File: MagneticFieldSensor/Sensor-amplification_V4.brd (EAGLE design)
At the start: 100 x 48.9 mm, 52 parts

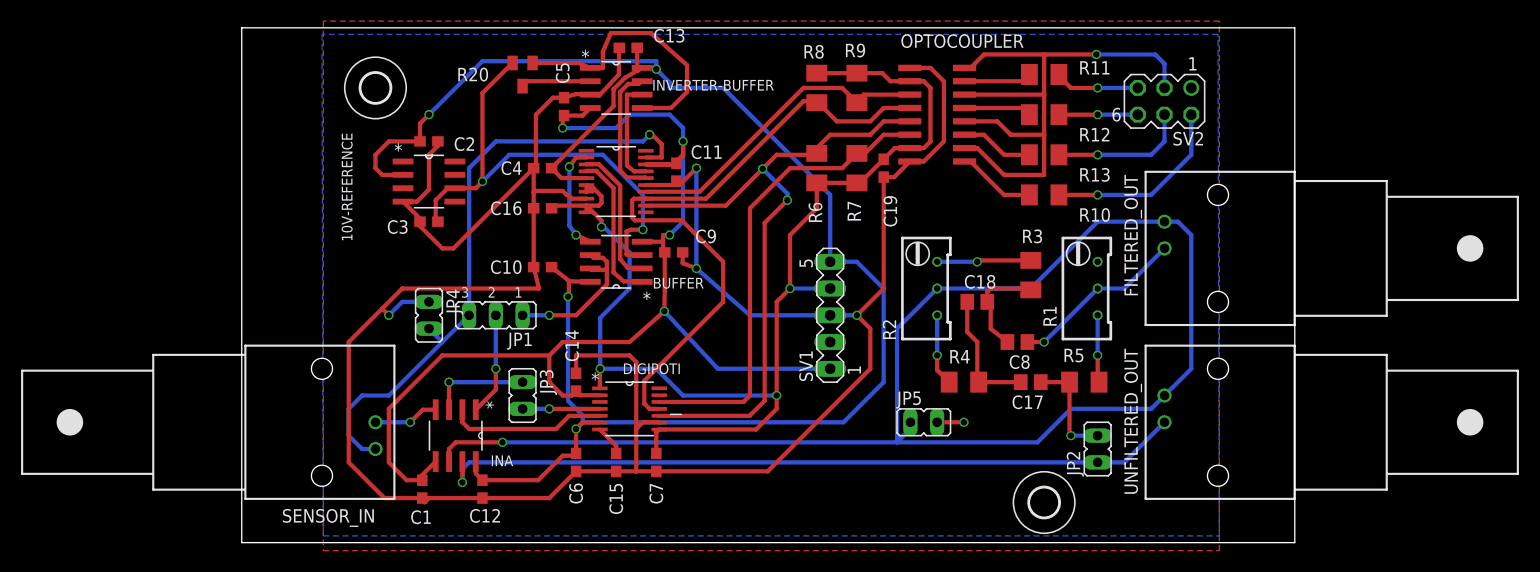
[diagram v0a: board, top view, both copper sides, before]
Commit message: made the board compatible with the PCB rules.
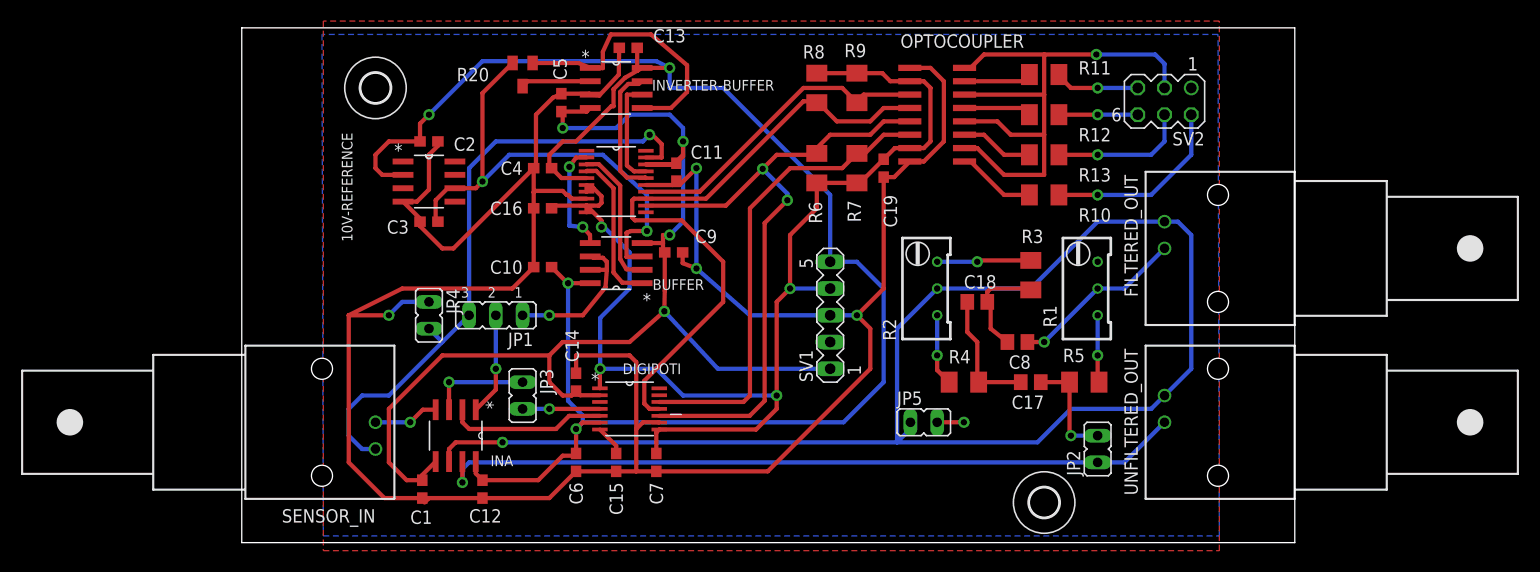
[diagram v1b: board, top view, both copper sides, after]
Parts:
- moved C5 0.46 mm to (30.4, 39.2)
- moved BUFFER 0.13 mm to (35.6, 24.0)
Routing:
- net +15V: track 166.1 -> 168.5 mm
- net AGND: track 247.7 -> 250.0 mm
- net N$9: track 46.4 -> 47.1 mm
